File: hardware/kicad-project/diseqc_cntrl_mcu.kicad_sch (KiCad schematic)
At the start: 44 parts, among them IC2 STM32F407VGT6, IC3 USBLC6-2P6, J3 Conn_01x04_Pin, J4 USB4110-GF-A, J9 Conn_ARM_SWD_TagConnect_TC2050, Y1 8MHZ

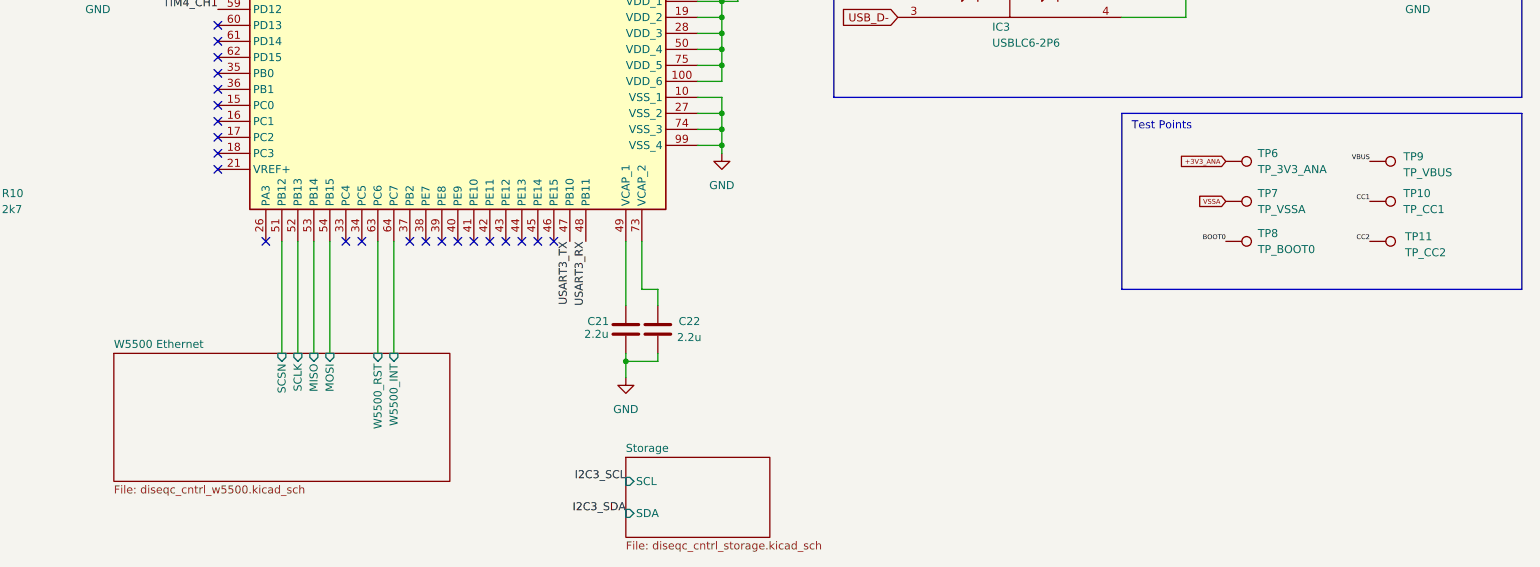
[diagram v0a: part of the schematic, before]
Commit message: Starting v0.4 with FT230 fixes; extra TPs
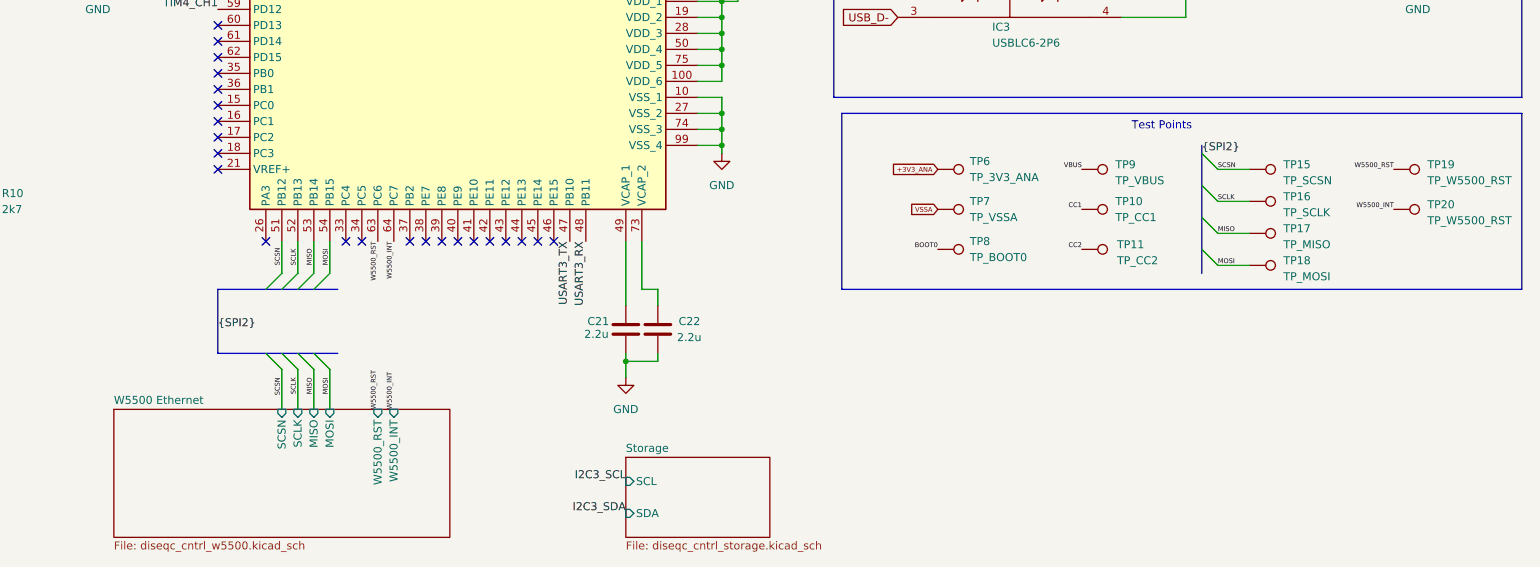
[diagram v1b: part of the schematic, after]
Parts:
- added TP15: TP_SCSN, TestPoint:TestPoint_THTPad_D1.0mm_Drill0.5mm, symbol Connector:TestPoint
- added TP16: TP_SCLK, TestPoint:TestPoint_THTPad_D1.0mm_Drill0.5mm, symbol Connector:TestPoint
- added TP17: TP_MISO, TestPoint:TestPoint_THTPad_D1.0mm_Drill0.5mm, symbol Connector:TestPoint
- added TP18: TP_MOSI, TestPoint:TestPoint_THTPad_D1.0mm_Drill0.5mm, symbol Connector:TestPoint
- added TP19, TP20: TP_W5500_RST, TestPoint:TestPoint_THTPad_D1.0mm_Drill0.5mm, symbol Connector:TestPoint
- C10, C7: InvenTree Part (none) -> C_1u_0603
- C11, C12, C14, C16, C17, C19, C20: InvenTree Part (none) -> C_100n_0603; Mouser Part Number 81-GRM39X104K16 -> (none)
- C13: InvenTree Part (none) -> C_10n_0603
- C15, C18: InvenTree Part (none) -> C_18p_0603
- C21, C22: InvenTree Part (none) -> C_2u2_0603
- C23: InvenTree Part (none) -> C_1n_0603
- C8: InvenTree Part (none) -> C_4u7_0603
- C9, J9, TP10, TP11, TP6, TP7, TP8, TP9: now left out of the parts list
- D3: InvenTree Part (none) -> LED_Green_0603
- IC2: InvenTree Part (none) -> IC_STM32F407VGT6_LQFP100
- IC3: InvenTree Part (none) -> D_ESD_5V_SOT_666_6
- J3: InvenTree Part (none) -> J_HDR_5x1_SMD
- J4: InvenTree Part (none) -> J_USB-C_SKT_16P
- L3: InvenTree Part (none) -> L_43n_0603
- R10, R9: InvenTree Part (none) -> R_2k7_0603
- R11: InvenTree Part (none) -> R_1k5_0603
- R12, R7, R8: InvenTree Part (none) -> R_4k7_0603
- R13, R6: InvenTree Part (none) -> R_10k_0603
- R14, R15: InvenTree Part (none) -> R_5k1_0603
- R31: InvenTree Part (none) -> R_100k_0603
- S1: InvenTree Part (none) -> J_SW_SPDT_SMD
- Y1: InvenTree Part (none) -> X_8MHZ
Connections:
- net W5500 Ethernet/MISO renamed MISO
- net MISO: now also TP17.1
- net W5500 Ethernet/MOSI renamed MOSI
- net MOSI: now also TP18.1
- net W5500 Ethernet/SCLK renamed SCLK
- net SCLK: now also TP16.1
- net W5500 Ethernet/SCSN renamed SCSN
- net SCSN: now also TP15.1
- net W5500 Ethernet/W5500_INT renamed W5500_INT
- net W5500_INT: now also TP20.1
- net W5500 Ethernet/W5500_RST renamed W5500_RST
- net W5500_RST: now also TP19.1
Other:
- moved on the sheet: TP10, TP11, TP6, TP7, TP8, TP9

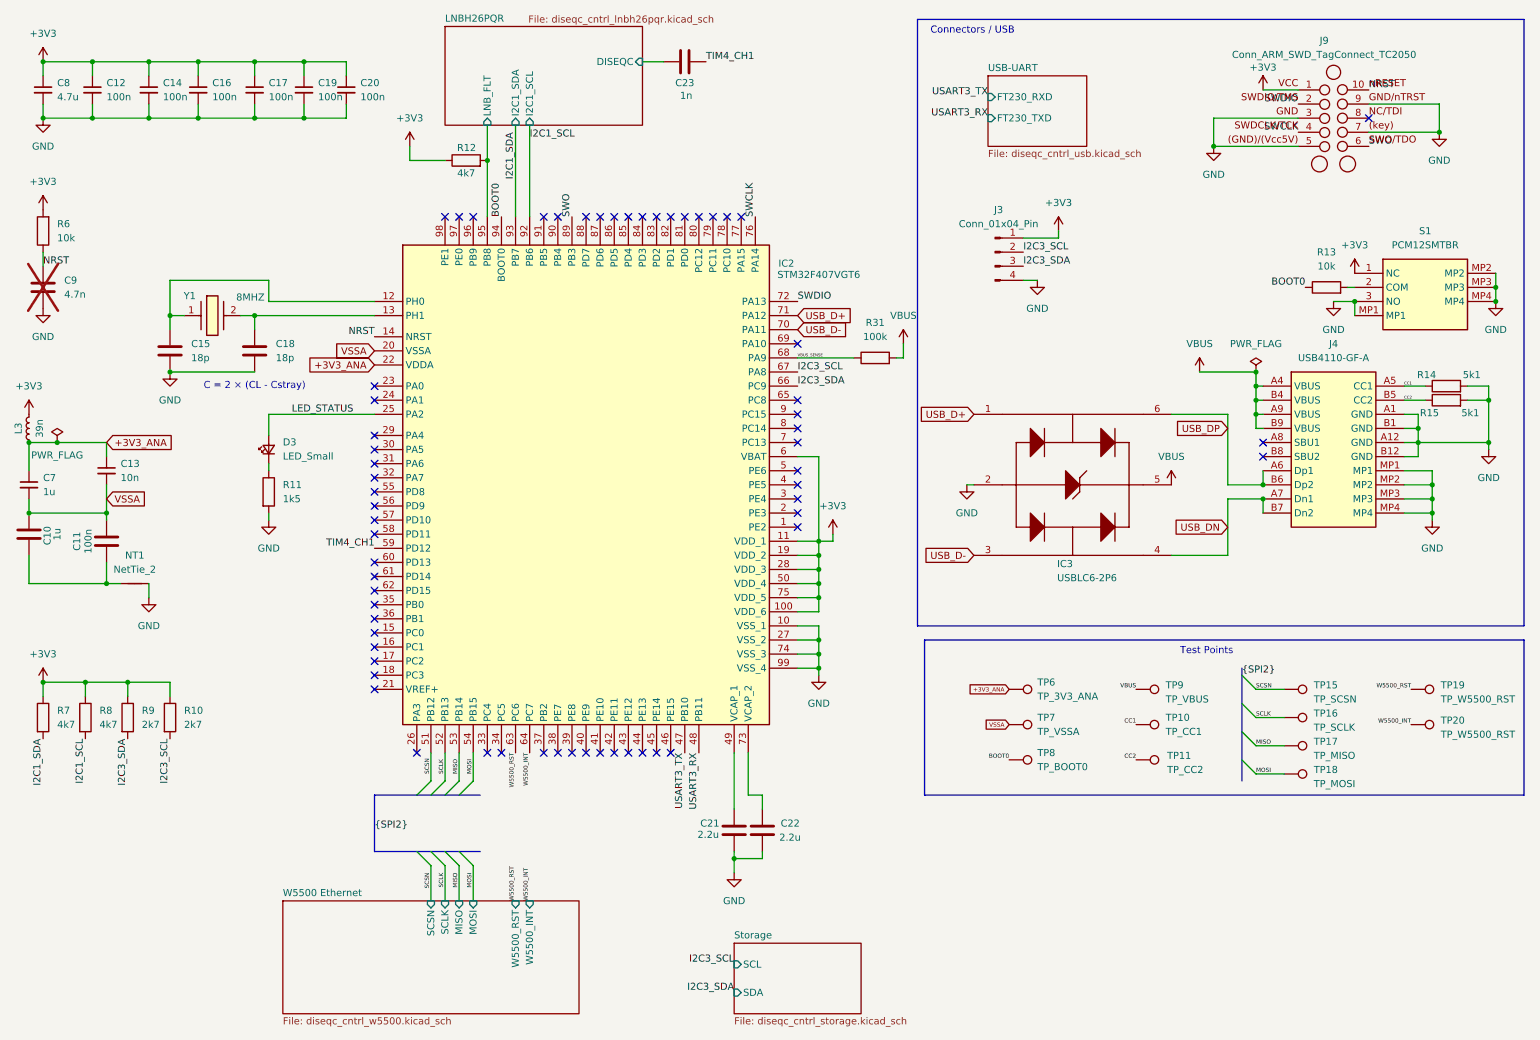
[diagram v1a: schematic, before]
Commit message: Removed separate VDDA/VSSA planes
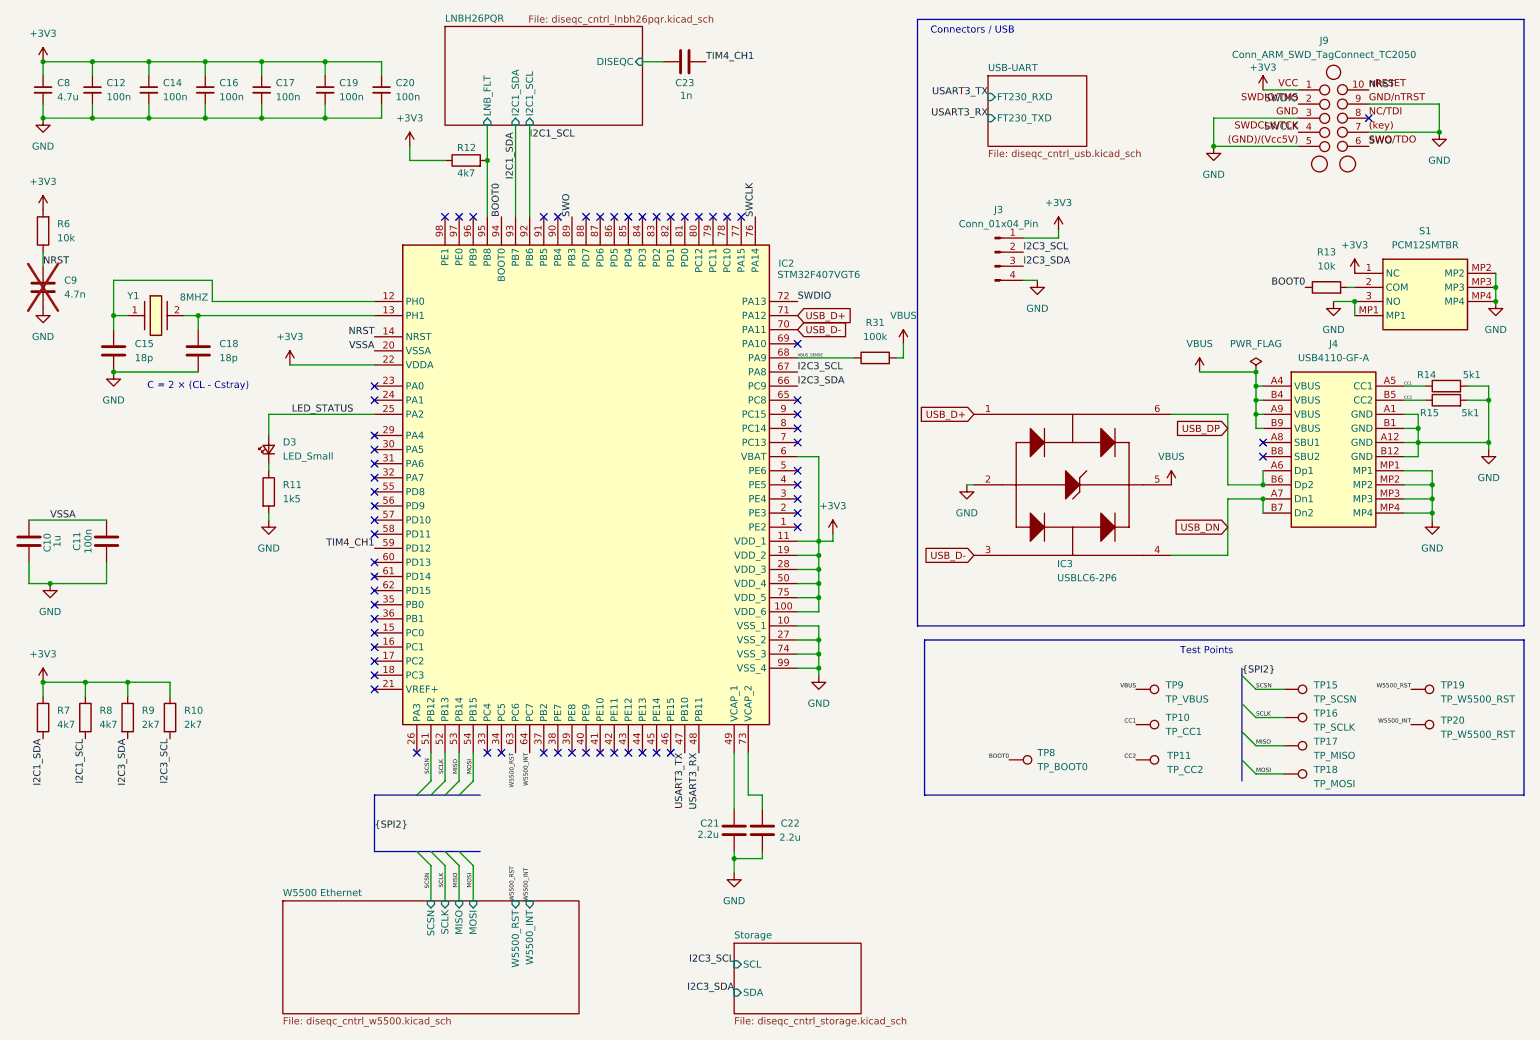
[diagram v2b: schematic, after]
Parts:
- removed C13: 10n, Capacitor_SMD:C_0603_1608Metric_Pad1.08x0.95mm_HandSolder, symbol diseqc_cntrl:C_Small
- removed C7: 1u, Capacitor_SMD:C_0603_1608Metric_Pad1.08x0.95mm_HandSolder, symbol diseqc_cntrl:C_Small
- removed L3: 39n, Inductor_SMD:L_0603_1608Metric_Pad1.05x0.95mm_HandSolder, symbol diseqc_cntrl:L_Small
- removed NT1: NetTie_2, NetTie:NetTie-2_SMD_Pad2.0mm, symbol diseqc_cntrl:NetTie_2
- removed TP6: TP_3V3_ANA, TestPoint:TestPoint_THTPad_D1.0mm_Drill0.5mm, symbol Connector:TestPoint
- removed TP7: TP_VSSA, TestPoint:TestPoint_THTPad_D1.0mm_Drill0.5mm, symbol Connector:TestPoint
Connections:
- net +3V3_ANA is gone; now on net +3V3: IC2.22 (VDDA)
- net GND: now also C10.2, C11.2
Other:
- moved on the sheet: C10, C15, C16, C17, C18, C19, C20, Y1

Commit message: Added InvenTree part codes
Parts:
- C10: InvenTree (none) -> 72
- C11, C12, C14, C16, C17, C19, C20: InvenTree (none) -> 75
- C15, C18: InvenTree (none) -> 66
- C21, C22: value 2.2u -> 2u2; InvenTree (none) -> 71
- C23: InvenTree (none) -> 73
- C8: InvenTree (none) -> 76
- D3: InvenTree (none) -> 99
- IC2: InvenTree (none) -> 102
- IC3: InvenTree (none) -> 129
- J3: InvenTree (none) -> 77
- J4: InvenTree (none) -> 82
- R10, R9: InvenTree (none) -> 109
- R11: InvenTree (none) -> 107
- R12, R7, R8: InvenTree (none) -> 113
- R13, R6: InvenTree (none) -> 106
- R14, R15: InvenTree (none) -> 111
- R31: InvenTree (none) -> 105
- S1: InvenTree (none) -> 121
- Y1: InvenTree (none) -> 84

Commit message: Corrected TP20 value
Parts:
- TP20: value TP_W5500_RST -> TP_W5500_INT
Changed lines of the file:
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@@
 	(title_block
 		(title "DiSEqc Motor Control")
+		(date "2026-06-09")
+		(rev "0.5-dev")
 		(company "M0DMF ")
 	)
@@
 			)
 		)
-		(property "Value" "TP_W5500_RST"
+		(property "Value" "TP_W5500_INT"
 			(at 269.494 144.018 90)
 			(show_name no)
